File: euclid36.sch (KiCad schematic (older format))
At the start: 24 parts, among them SW1 SW_Push, U1 ATmega32U4-AU, Y1 Crystal_GND24_Small

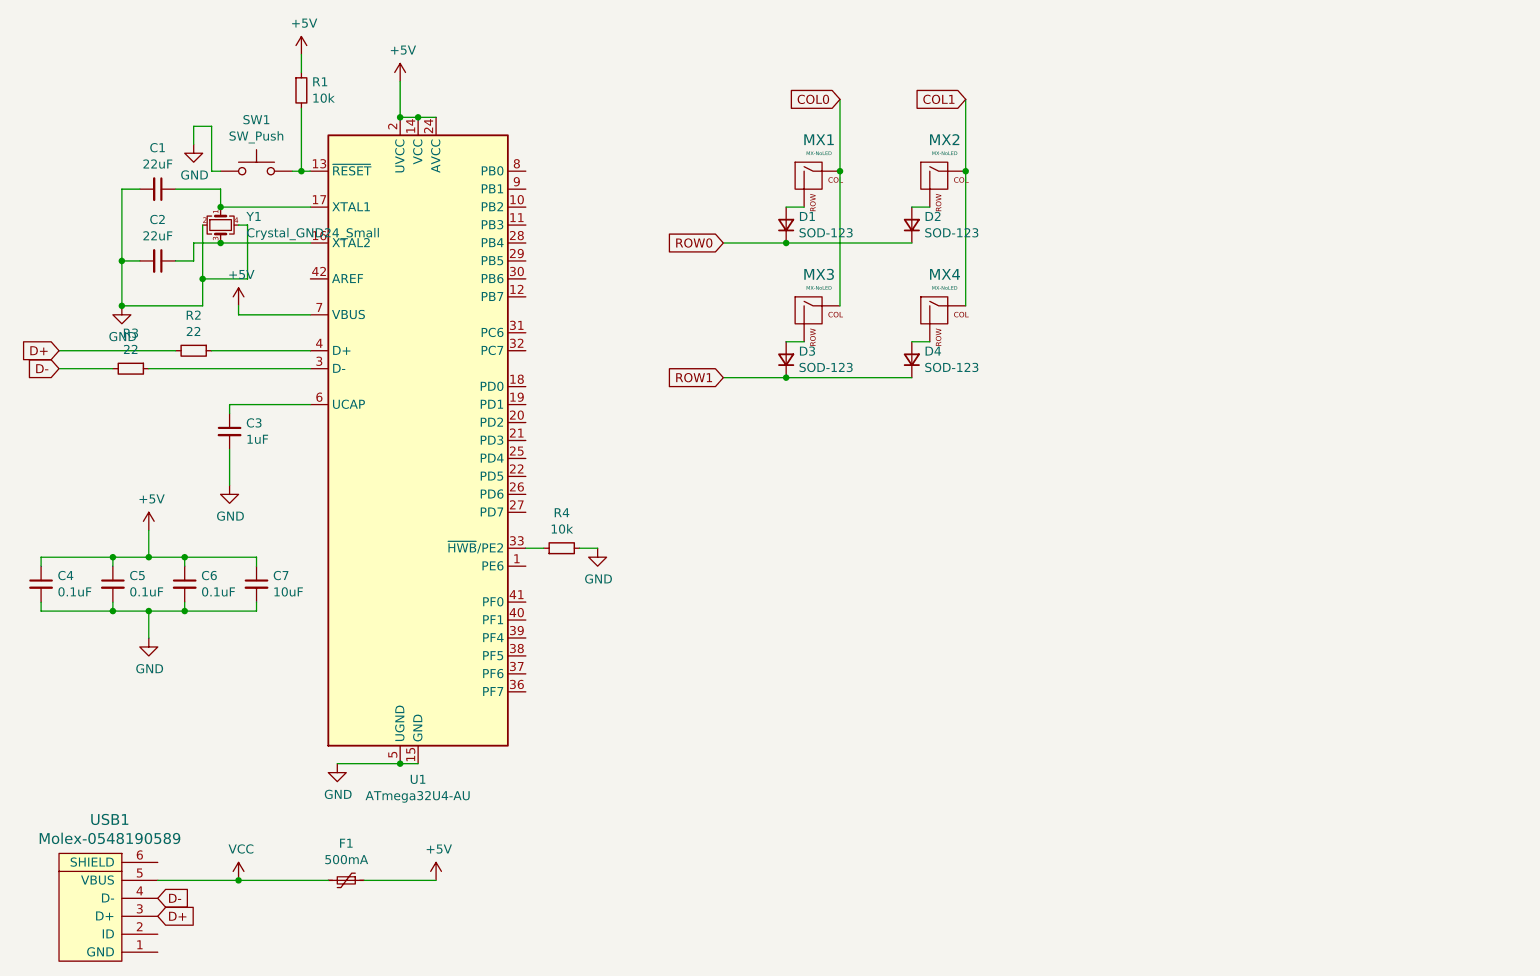
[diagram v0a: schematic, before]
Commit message: Added all 36 keys
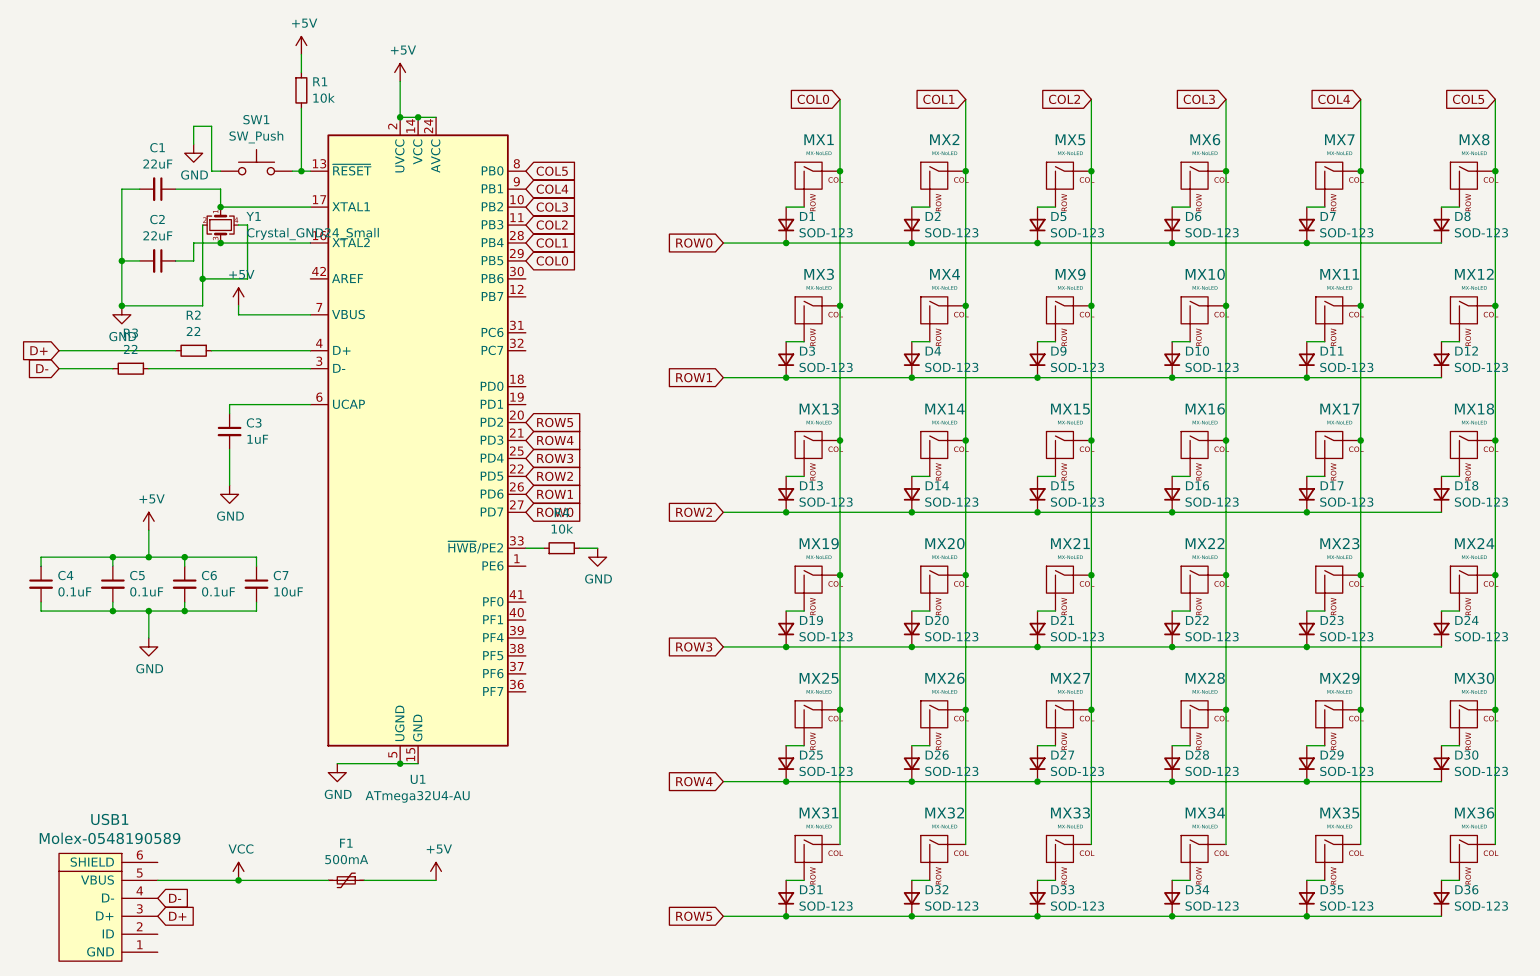
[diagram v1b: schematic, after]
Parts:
- added D10, D11, D12, D13, D14, D15, D16, D17, D18, D19, D20, D21, D22, D23, D24, D25, D26, D27, D28, D29, D30, D31, D32, D33, D34, D35, D36, D5, D6, D7, D8, D9: SOD-123, Diode_SMD:D_SOD-123, symbol euclid36-rescue:D_Small-Device
- added MX10, MX11, MX12, MX13, MX14, MX15, MX16, MX17, MX18, MX19, MX20, MX21, MX22, MX23, MX24, MX25, MX26, MX27, MX28, MX29, MX30, MX31, MX32, MX33, MX34, MX35, MX36, MX5, MX6, MX7, MX8, MX9: MX-NoLED, MX_Alps_Hybrid:MXOnly-1U-Hotswap, symbol MX_Alps_Hybrid:MX-NoLED
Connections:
- net COL0: now also U1.29 (PB5), MX13.1 (COL), MX19.1 (COL), MX25.1 (COL), MX31.1 (COL)
- net COL1: now also U1.28 (PB4), MX14.1 (COL), MX20.1 (COL), MX26.1 (COL), MX32.1 (COL)
- net ROW0: now also U1.27 (PD7), D5.1 (K), D6.1 (K), D7.1 (K), D8.1 (K)
- net ROW1: now also U1.26 (PD6), D10.1 (K), D11.1 (K), D12.1 (K), D9.1 (K)
- net COL3: now reaches U1.10 (PB2)
- net COL3: now also MX10.1 (COL), MX16.1 (COL), MX22.1 (COL), MX28.1 (COL), MX34.1 (COL), MX6.1 (COL)
- net COL2: now reaches U1.11 (PB3)
- net COL2: now also MX15.1 (COL), MX21.1 (COL), MX27.1 (COL), MX33.1 (COL), MX5.1 (COL), MX9.1 (COL)
- net ROW5: now reaches U1.20 (PD2)
- net ROW5: now also D31.1 (K), D32.1 (K), D33.1 (K), D34.1 (K), D35.1 (K), D36.1 (K)
- net ROW4: now reaches U1.21 (PD3)
- net ROW4: now also D25.1 (K), D26.1 (K), D27.1 (K), D28.1 (K), D29.1 (K), D30.1 (K)
- net ROW2: now reaches U1.22 (PD5)
- net ROW2: now also D13.1 (K), D14.1 (K), D15.1 (K), D16.1 (K), D17.1 (K), D18.1 (K)
- net ROW3: now reaches U1.25 (PD4)
- net ROW3: now also D19.1 (K), D20.1 (K), D21.1 (K), D22.1 (K), D23.1 (K), D24.1 (K)
- net COL5: now reaches U1.8 (PB0)
- net COL5: now also MX12.1 (COL), MX18.1 (COL), MX24.1 (COL), MX30.1 (COL), MX36.1 (COL), MX8.1 (COL)
- net COL4: now reaches U1.9 (PB1)
- net COL4: now also MX11.1 (COL), MX17.1 (COL), MX23.1 (COL), MX29.1 (COL), MX35.1 (COL), MX7.1 (COL)
- new net: D5.2 (A), MX5.2 (ROW)
- new net: D6.2 (A), MX6.2 (ROW)
- new net: D7.2 (A), MX7.2 (ROW)
- new net: D8.2 (A), MX8.2 (ROW)
- new net: D9.2 (A), MX9.2 (ROW)
- new net: D10.2 (A), MX10.2 (ROW)
- new net: D11.2 (A), MX11.2 (ROW)
- new net: D12.2 (A), MX12.2 (ROW)
- new net: D15.2 (A), MX15.2 (ROW)
- new net: D16.2 (A), MX16.2 (ROW)
- new net: D17.2 (A), MX17.2 (ROW)
- new net: D18.2 (A), MX18.2 (ROW)
- new net: D13.2 (A), MX13.2 (ROW)
- new net: D14.2 (A), MX14.2 (ROW)
- new net: D20.2 (A), MX20.2 (ROW)
- new net: D19.2 (A), MX19.2 (ROW)
- new net: D24.2 (A), MX24.2 (ROW)
- new net: D23.2 (A), MX23.2 (ROW)
- new net: D22.2 (A), MX22.2 (ROW)
- new net: D21.2 (A), MX21.2 (ROW)
- new net: D26.2 (A), MX26.2 (ROW)
- new net: D25.2 (A), MX25.2 (ROW)
- new net: D30.2 (A), MX30.2 (ROW)
- new net: D29.2 (A), MX29.2 (ROW)
- new net: D28.2 (A), MX28.2 (ROW)
- new net: D27.2 (A), MX27.2 (ROW)
- new net: D32.2 (A), MX32.2 (ROW)
- new net: D31.2 (A), MX31.2 (ROW)
- new net: D36.2 (A), MX36.2 (ROW)
- new net: D35.2 (A), MX35.2 (ROW)
- new net: D34.2 (A), MX34.2 (ROW)
- new net: D33.2 (A), MX33.2 (ROW)

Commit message: Updated key switch and diode labels
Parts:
- renumbered D6 to D10, D10 to D11, D16 to D12, D7 to D13, D11 to D14, D17 to D15, D19 to D16, D25 to D17, D31 to D18, D20 to D19, D3 to D2, D26 to D20, D32 to D21, D21 to D22, D27 to D23, D33 to D24, D22 to D25, D28 to D26, D34 to D27, D23 to D28, D13 to D3, D35 to D30, D8 to D31, D12 to D32, D18 to D33, D24 to D34, D30 to D35, D2 to D4, D4 to D5, D14 to D6, D5 to D7, D9 to D8, D15 to D9, MX6 to MX10, MX10 to MX11, MX16 to MX12, MX7 to MX13, MX11 to MX14, MX17 to MX15, MX19 to MX16, MX25 to MX17, MX31 to MX18, MX20 to MX19, MX3 to MX2, MX26 to MX20, MX32 to MX21, MX21 to MX22, MX27 to MX23, MX33 to MX24, MX22 to MX25, MX28 to MX26, MX34 to MX27, MX23 to MX28, MX13 to MX3, MX35 to MX30, MX8 to MX31, MX12 to MX32, MX18 to MX33, MX24 to MX34, MX30 to MX35, MX2 to MX4, MX4 to MX5, MX14 to MX6, MX5 to MX7, MX9 to MX8, MX15 to MX9
